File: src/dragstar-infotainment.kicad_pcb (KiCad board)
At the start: 2 copper layers, 100 x 97 mm, 142 parts, among them J1 MiniFit_2x10_F, J1 XT60-M, J10 Conn_01x01_Socket, J100 Conn_01x01_Socket, J101 1217080-1, J102 1217080-1, J103 1217080-1, J104 1217080-1, J105 1217080-1, J106 1217080-1, J107 1217080-1, J108 1217080-1, J109 1217080-1, J11 Conn_01x01_Socket, J110 1217080-1, J111 1217080-1, J112 1217080-1, J12 Conn_01x01_Socket, J13 Conn_01x01_Socket, J14 Conn_01x01_Socket, J15 Conn_01x01_Socket, J16 Conn_01x01_Socket, J17 Conn_01x01_Socket, J18 Conn_01x01_Socket, J19 Conn_01x01_Socket, J20 Conn_01x01_Socket, J21 Conn_01x01_Socket, J22 Conn_01x01_Socket, J23 Conn_01x01_Socket, J24 Conn_01x01_Socket, J25 Conn_01x01_Socket, J26 Conn_01x01_Socket, J27 Conn_01x01_Socket, J28 Conn_01x01_Socket, J29 Conn_01x01_Socket, J3 Conn_01x01_Socket, J30 Conn_01x01_Socket, J31 Conn_01x01_Socket, J32 Conn_01x01_Socket, J33 Conn_01x01_Socket, J34 Conn_01x01_Socket, J35 Conn_01x01_Socket, J36 Conn_01x01_Socket, J37 Conn_01x01_Socket, J38 Conn_01x01_Socket, J39 Conn_01x01_Socket, J4 1217080-1, J4 Conn_01x01_Socket, J40 Conn_01x01_Socket, J41 MiniFit_2x03_F, J42 MiniFit_2x03_F, J43 MiniFit_2x03_F, J44 MiniFit_2x03_F, J45 MiniFit_2x04_M, J46 MiniFit_2x02_F, J47 MiniFit_2x04_F, J5 Conn_01x01_Socket, J50 USB_A, J51 MiniFit_2x01_M, J52 MiniFit_2x01_M, J53 MiniFit_2x03_F, J6 Conn_01x01_Socket, J69 MiniFit_2x04_M, J7 Conn_01x01_Socket, J8 Conn_01x01_Socket, J84 MiniFit_2x02_M, J85 MiniFit_2x03_M, J86 MiniFit_2x01_F, J87 MiniFit_2x01_F, J88 MiniFit_2x04_M, J89 1217080-1, J9 Conn_01x01_Socket, J91 Barrel_Jack, J92 MiniFit_2x03_M, J93 MiniFit_2x03_M, J94 Barrel_Jack, J96 MiniFit_2x03_M, J97 MiniFit_2x03_M, J98 Conn_01x01_Socket, J99 Conn_01x01_Socket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

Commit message: simplify circuit diagram. Remove unecessary features; Split board into two components|
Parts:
- removed D10, D11, D12, D9: US1M, Diode_SMD:D_SMA
- removed the J1 at (118.2, 148.0)
- removed the J1 at (108.6, 66.6)
- removed J100, J14, J15, J16, J17, J18, J19, J20, J21, J22, J23, J24, J25, J26, J27, J28, J29, J30, J31, J32, J33, J34, J35, J36, J37, J40, J98, J99: Conn_01x01_Socket, Connector_Pin:Pin_D1.0mm_L10.0mm
- removed J101, J102, J103, J104, J105, J106, J107, J108, J109, J110, J111, J112, J89: 1217080-1, SamacSys_Parts:1217080-1
- removed the J4 at (125.0, 150.8)
- removed the J4 at (112.8, 77.2)
- removed J41, J42, J53: MiniFit_2x03_F, Connector_Molex:Molex_Mini-Fit_Jr_5566-06A_2x03_P4.20mm_Vertical
- removed J45, J88: MiniFit_2x04_M, Connector_Molex:Molex_Mini-Fit_Jr_5566-08A_2x04_P4.20mm_Vertical
- removed J46: MiniFit_2x02_F, Connector_Molex:Molex_Mini-Fit_Jr_5566-04A_2x02_P4.20mm_Vertical
- removed J47: MiniFit_2x04_F, Connector_Molex:Molex_Mini-Fit_Jr_5566-08A_2x04_P4.20mm_Vertical
- removed J50: USB_A, Connector_USB:USB_A_Molex_67643_Horizontal
- removed J51, J52: MiniFit_2x01_M, Connector_Molex:Molex_Mini-Fit_Jr_5566-02A_2x01_P4.20mm_Vertical
- removed J84: MiniFit_2x02_M, Connector_Molex:Molex_Mini-Fit_Jr_5566-04A_2x02_P4.20mm_Vertical
- removed J85, J92, J93, J96, J97: MiniFit_2x03_M, Connector_Molex:Molex_Mini-Fit_Jr_5566-06A_2x03_P4.20mm_Vertical
- removed J86, J87: MiniFit_2x01_F, Connector_Molex:Molex_Mini-Fit_Jr_5566-02A_2x01_P4.20mm_Vertical
- removed J91, J94: Barrel_Jack, Connector_BarrelJack:BarrelJack_CUI_PJ-063AH_Horizontal
- removed the R2 at (132.7, 123.5)
- removed the R2 at (132.6, 117.8)
- removed the R3 at (126.3, 118.8)
- removed the R3 at (132.7, 125.8)
- removed R6, R7: 10K, Resistor_SMD:R_1206_3216Metric_Pad1.30x1.75mm_HandSolder
- removed R8, R9: 470R, Resistor_THT:R_Axial_DIN0204_L3.6mm_D1.6mm_P5.08mm_Horizontal
- added A1: Mini360_3A, Local Footprints:Mini360_DC_DC_Buck_Converter, F.Cu at (42.8, 124.2)
- added A2: Mini360_3A, Local Footprints:Mini360_DC_DC_Buck_Converter, F.Cu at (42.8, 137.2)
- added C1: 0.01µF, Capacitor_SMD:C_1206_3216Metric_Pad1.33x1.80mm_HandSolder, F.Cu at (69.5, 140.9)
- added C2: 100µF, Capacitor_SMD:C_Elec_8x6.2, F.Cu at (77.8, 133.2)
- added C3: 0.1µF, Capacitor_SMD:C_1206_3216Metric_Pad1.33x1.80mm_HandSolder, B.Cu at (80.2, 135.7)
- added C4: 0.1µF, Capacitor_SMD:C_1206_3216Metric_Pad1.33x1.80mm_HandSolder, B.Cu at (76.0, 144.4)
- added C5: 100µF, Capacitor_SMD:C_Elec_8x6.2, F.Cu at (210.2, 55.2)
- added C6: 0.1µF, Capacitor_SMD:C_1206_3216Metric_Pad1.33x1.80mm_HandSolder, F.Cu at (216.8, 57.2)
- added C7: 100µF, Capacitor_SMD:C_Elec_8x6.2, F.Cu at (62.8, 63.7)
- added C8: 22µF, Capacitor_SMD:C_Elec_6.3x5.4, F.Cu at (62.5, 54.0)
- added D30: US1M, Diode_SMD:D_SMA, B.Cu at (93.1, 59.4)
- added D31: 2.7V, Diode_THT:D_DO-35_SOD27_P7.62mm_Horizontal, F.Cu at (110.5, 61.2)
- added D32: US1M, Diode_SMD:D_SMA, F.Cu at (64.8, 119.7)
- added D33: US1M, Diode_SMD:D_SMA, F.Cu at (64.8, 123.4)
- added D34: US1M, Diode_SMD:D_SMA, F.Cu at (64.8, 126.9)
- added D35: US1M, Diode_SMD:D_SMA, F.Cu at (64.8, 140.2)
- added D36: US1M, Diode_SMD:D_SMA, F.Cu at (64.8, 136.8)
- added D37: US1M, Diode_SMD:D_SMA, F.Cu at (64.8, 133.2)
- added H1: MountingHole_Pad, MountingHole:MountingHole_3.2mm_M3_DIN965_Pad, F.Cu at (109.8, 54.2)
- added H2: MountingHole_Pad, MountingHole:MountingHole_3.2mm_M3_DIN965_Pad, F.Cu at (109.8, 144.2)
- added H3: MountingHole_Pad, MountingHole:MountingHole_3.2mm_M3_DIN965_Pad, F.Cu at (44.8, 54.2)
- added H4: MountingHole_Pad, MountingHole:MountingHole_3.2mm_M3_DIN965_Pad, F.Cu at (44.8, 144.2)
- added J1: Conn_01x01, TestPoint:TestPoint_THTPad_D2.5mm_Drill1.2mm, F.Cu at (74.5, 103.0)
- added J2: Conn_01x01, TestPoint:TestPoint_THTPad_D2.5mm_Drill1.2mm, F.Cu at (74.5, 112.0)
- added J4: Conn_01x01, TestPoint:TestPoint_THTPad_D2.5mm_Drill1.2mm, F.Cu at (70.2, 99.3)
- added J61: Conn_01x01, MountingHole:MountingHole_3.2mm_M3_DIN965_Pad, F.Cu at (53.9, 54.5)
- added J62: Conn_01x01, MountingHole:MountingHole_3.2mm_M3_DIN965_Pad, F.Cu at (84.0, 89.0)
- added J63: Conn_01x01, TestPoint:TestPoint_THTPad_D2.5mm_Drill1.2mm, F.Cu at (80.9, 57.3)
- added J64: 1217080-1, SamacSys_Parts:1217080-1, F.Cu at (72.8, 86.6)
- added J65: 1217080-1, SamacSys_Parts:1217080-1, F.Cu at (72.8, 78.4)
- added J66: 1217080-1, SamacSys_Parts:1217080-1, F.Cu at (89.5, 98.0)
- added J67: 1217080-1, SamacSys_Parts:1217080-1, F.Cu at (89.5, 128.0)
- added J68: 1217080-1, SamacSys_Parts:1217080-1, F.Cu at (89.5, 108.0)
- added J70: 1217080-1, SamacSys_Parts:1217080-1, F.Cu at (97.7, 138.0)
- added J71: 1217080-1, SamacSys_Parts:1217080-1, F.Cu at (97.7, 98.0)
- added J72: 1217080-1, SamacSys_Parts:1217080-1, F.Cu at (97.7, 128.0)
- added J73: 1217080-1, SamacSys_Parts:1217080-1, F.Cu at (97.7, 108.0)
- added J74: 1217080-1, SamacSys_Parts:1217080-1, F.Cu at (97.8, 118.0)
- added J75: 1217080-1, SamacSys_Parts:1217080-1, F.Cu at (89.5, 138.0)
- added L2: 22µH, Inductor_THT:L_Toroid_Vertical_L17.8mm_W9.7mm_P7.11mm_Pulse_B, F.Cu at (69.4, 63.7)
- added R2: 1K, Resistor_SMD:R_1206_3216Metric_Pad1.30x1.75mm_HandSolder, B.Cu at (68.0, 132.0)
- added R21: 10K, Resistor_SMD:R_1206_3216Metric_Pad1.30x1.75mm_HandSolder, F.Cu at (204.0, 79.5)
- added R23: 10K, Resistor_SMD:R_1206_3216Metric_Pad1.30x1.75mm_HandSolder, B.Cu at (95.5, 64.0)
- added R3: 10K, Resistor_SMD:R_1206_3216Metric_Pad1.30x1.75mm_HandSolder, B.Cu at (61.0, 130.6)
- added RV1: 10K-50K, Potentiometer_THT:Potentiometer_Bourns_3386P_Vertical, F.Cu at (55.5, 145.5)
- D1, D2, D7, R5: moved to B.Cu
- D13, D4: footprint Diode_SMD:D_MiniMELF -> Diode_THT:D_DO-35_SOD27_P7.62mm_Horizontal
- D14: value US1M -> 1N4001; footprint Diode_SMD:D_SMA -> Diode_THT:D_DO-41_SOD81_P10.16mm_Horizontal; moved to F.Cu
- D15, D16: value 2.7V -> 1N4001; footprint Diode_SMD:D_MiniMELF -> Diode_THT:D_DO-41_SOD81_P10.16mm_Horizontal; moved to F.Cu
- D17: value LED -> 1N4001; footprint LED_THT:LED_D5.0mm -> Diode_THT:D_DO-41_SOD81_P10.16mm_Horizontal
- D18, D19: value LED -> 2.7V; footprint LED_THT:LED_D5.0mm -> Diode_THT:D_DO-35_SOD27_P7.62mm_Horizontal
- D20: value LED -> US1M; footprint LED_THT:LED_D5.0mm -> Diode_SMD:D_SMA
- D21: value LED Green -> US1M; footprint LED_THT:LED_D5.0mm -> Diode_SMD:D_SMA
- D22: value LED Blue -> US1M; footprint LED_THT:LED_D5.0mm -> Diode_SMD:D_SMA
- D23: value LED Red -> 10V; footprint LED_THT:LED_D5.0mm -> Diode_THT:D_DO-35_SOD27_P7.62mm_Horizontal
- D24: value LED Yellow -> LED_Dual_AKA (Green, Red); footprint LED_THT:LED_D5.0mm -> LED_THT:LED_D5.0mm-3
- D26: value US1M -> LED Blue; footprint Diode_SMD:D_SMA -> LED_THT:LED_D5.0mm; moved to F.Cu
- D27: value 2.7V -> LED Red; footprint Diode_SMD:D_MiniMELF -> LED_THT:LED_D5.0mm; moved to F.Cu
- D28: value 10V -> LED Green; footprint Diode_SMD:D_MiniMELF -> LED_THT:LED_D5.0mm
- D3, D6: footprint Diode_SMD:D_MiniMELF -> Diode_THT:D_DO-35_SOD27_P7.62mm_Horizontal; moved to F.Cu
- D8: value US1M -> 2.7V; footprint Diode_SMD:D_SMA -> Diode_THT:D_DO-35_SOD27_P7.62mm_Horizontal
- J10, J11, J12, J3, J5, J6, J7, J8, J9: value Conn_01x01_Socket -> Conn_01x01; footprint Connector_Pin:Pin_D1.0mm_L10.0mm -> TestPoint:TestPoint_THTPad_D2.5mm_Drill1.2mm; moved to F.Cu
- J13: value Conn_01x01_Socket -> XT60-M; footprint Connector_Pin:Pin_D1.0mm_L10.0mm -> Local Footprints:AMASS_XT60PW-M_1x02_P7.20mm_Horizontal_Short; moved to F.Cu
- J38, J39: value Conn_01x01_Socket -> JST XH 6 Pins; footprint Connector_Pin:Pin_D1.0mm_L10.0mm -> Connector_JST:JST_XH_B6B-XH-A_1x06_P2.50mm_Vertical
- J43, J44: value MiniFit_2x03_F -> Conn_01x01; footprint Connector_Molex:Molex_Mini-Fit_Jr_5566-06A_2x03_P4.20mm_Vertical -> TestPoint:TestPoint_THTPad_D2.5mm_Drill1.2mm
- J69: value MiniFit_2x04_M -> 1217080-1; footprint Connector_Molex:Molex_Mini-Fit_Jr_5566-08A_2x04_P4.20mm_Vertical -> SamacSys_Parts:1217080-1
- Q5, Q6: value 2N7002 -> AO3413; moved to F.Cu
- Q7: value BC557 -> 2N7002; footprint Package_TO_SOT_THT:TO-92_Inline -> Package_TO_SOT_SMD:SOT-23; moved to B.Cu
- R10, R11: value 470R -> 10K; footprint Resistor_THT:R_Axial_DIN0204_L3.6mm_D1.6mm_P5.08mm_Horizontal -> Resistor_SMD:R_1206_3216Metric_Pad1.30x1.75mm_HandSolder
- R12: value 680R -> 10K; footprint Resistor_THT:R_Axial_DIN0204_L3.6mm_D1.6mm_P5.08mm_Horizontal -> Resistor_SMD:R_1206_3216Metric_Pad1.30x1.75mm_HandSolder
- R13: value 680R -> 100; footprint Resistor_THT:R_Axial_DIN0204_L3.6mm_D1.6mm_P5.08mm_Horizontal -> Resistor_SMD:R_1206_3216Metric_Pad1.30x1.75mm_HandSolder
- R14: value 680R -> 1.5K; footprint Resistor_THT:R_Axial_DIN0204_L3.6mm_D1.6mm_P5.08mm_Horizontal -> Resistor_SMD:R_1206_3216Metric_Pad1.30x1.75mm_HandSolder
- R17: value 10K -> 680R; footprint Resistor_SMD:R_1206_3216Metric_Pad1.30x1.75mm_HandSolder -> Resistor_THT:R_Axial_DIN0204_L3.6mm_D1.6mm_P5.08mm_Horizontal; moved to F.Cu
- R18: value 100 -> 680R; footprint Resistor_SMD:R_1206_3216Metric_Pad1.30x1.75mm_HandSolder -> Resistor_THT:R_Axial_DIN0204_L3.6mm_D1.6mm_P5.08mm_Horizontal
- R19: value 1.5K -> 680R; footprint Resistor_SMD:R_1206_3216Metric_Pad1.30x1.75mm_HandSolder -> Resistor_THT:R_Axial_DIN0204_L3.6mm_D1.6mm_P5.08mm_Horizontal
- R20: value 10K -> 680R; footprint Resistor_SMD:R_1206_3216Metric_Pad1.30x1.75mm_HandSolder -> Resistor_THT:R_Axial_DIN0204_L3.6mm_D1.6mm_P5.08mm_Horizontal
- moved J69 344.8 mm to (89.5, 118.0)
- moved D20 290.7 mm to (211.5, 84.5)
- moved D19 290.5 mm to (197.6, 73.8), turned to 90 degrees
- moved D18 272.4 mm to (205.1, 63.8), turned to 180 degrees
- moved D17 262.6 mm to (200.0, 48.0), turned to -90 degrees
- moved R11 260.6 mm to (203.4, 66.5)
- moved R10 250.2 mm to (218.3, 68.3), turned to 90 degrees
- moved J43 245.3 mm to (209.6, 80.8), turned to 90 degrees
- moved J44 234.6 mm to (214.1, 80.8), turned to 90 degrees
- moved D25 215.4 mm to (220.8, 108.3), turned to 180 degrees
- moved D23 210.2 mm to (197.3, 82.2)
- moved D22 204.9 mm to (198.2, 87.2), turned to 90 degrees
- moved R14 203.3 mm to (197.6, 77.5), turned to -90 degrees
- moved R13 202.0 mm to (200.1, 77.3), turned to 90 degrees
- moved R12 201.2 mm to (200.1, 72.0), turned to -90 degrees
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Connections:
- D13 pad 1: /Main board/XOR 74LS00/B -> /Accessories/XOR 74LS00/A
- D14 pad 1: AuxSwitch -> RBlinker
- D14 pad 2: Net-(D14-A) -> Hazard
- D15 pad 1: Net-(D15-K) -> RBlinker
- D15 pad 2: GND -> Hazard
- D16 pad 1: Net-(D16-K) -> LBlinker
- D16 pad 2: GND -> Hazard
- D17 pad 1: GNDDash -> LBlinker
- D17 pad 2: Net-(D17-A) -> Hazard
- D18 pad 1: HazardLed -> /Accessories/XOR 74LS00/B
- D18 pad 2: Net-(D18-A) -> GND
- D19 pad 1: GNDDash -> Net-(D19-K)
- D19 pad 2: Net-(D19-A) -> GND
- D20 pad 1: GNDDash -> AuxLed2
- D20 pad 2: Net-(D20-A) -> AuxHBeam
- D21 pad 1: GNDDash -> AuxLed1
- D21 pad 2: Net-(D21-A) -> AuxHBeam
- D22 pad 1: GNDDash -> AuxLed1
- D22 pad 2: Net-(D22-A) -> AuxLBeam
- D23 pad 1: GNDDash -> Net-(D23-K)
- D24 pad 1: GNDDash -> Net-(D24-A1)
- D24 pad 2: Net-(D24-A) -> GNDDash
- D26 pad 1: +BATT -> GNDDash
- D27 pad 1: Net-(D27-K) -> GNDDash
- D27 pad 2: GND -> Net-(D27-A)
- D28 pad 1: Net-(D28-K) -> GNDDash
- D4 pad 1: PLightSignal -> Net-(D4-K)
- D7 pad 1: RBlinker -> AuxSwitch
- D7 pad 2: Hazard -> Net-(D7-A)
- D8 pad 1: RBlinker -> Net-(D8-K)
- D8 pad 2: Hazard -> GND
- J10 pad 1: Hazard -> AuxLBeam
- J11 pad 1: LBlinker -> AuxHBeam
- J12 pad 1: RBlinker -> AuxSwitch
- J13 pad 1: Key -> GND
- J3 pad 1: AuxLBeam -> Key
- J38 pad 1: GNDDash -> VInst
- J39 pad 1: PLight -> LBlinker
- J44 pad 1: VInst -> GND
- J5 pad 1: AuxHBeam -> HBeam
- J6 pad 1: HBeam -> PLight
- J69 pad 1: Accessory -> VLight
- J69 pad 2: HBeam -> VLight
- J7 pad 1: AuxBeams -> +5V
- J8 pad 1: AuxSwitch -> VOutlet
- J9 pad 1: HazardLed -> GNDDash
- K2 pad A1: Net-(D14-A) -> Net-(D7-A)
- K3 pad 14: +BATT -> MainRelay
- K3 pad A1: +BATT -> MainRelay
- K3 pad A2: Net-(D26-A) -> /Main board/Power Delivery/RelayGnd
- Q1 pad 3: GndDimmer -> Net-(Q1-D)
- Q2 pad 1: PLightSignal -> Net-(D4-K)
- Q2 pad 2: GndDimmer -> Net-(Q1-D)
- Q4 pad 1: Net-(D15-K) -> Net-(D8-K)
- Q4 pad 3: Net-(D14-A) -> Net-(D7-A)
- Q5 pad 1: Net-(D16-K) -> Net-(D19-K)
- Q5 pad 3: GndDimmer -> VInst
- Q6 pad 1: Net-(D27-K) -> Net-(D23-A)
- Q6 pad 2: GND -> LowBat
- Q6 pad 3: Net-(D26-A) -> VInst
- Q7 pad 1: +BATT -> Net-(D31-K)
- Q7 pad 2: Net-(D28-A) -> GND
- Q7 pad 3: LowBat -> /Main board/Power Delivery/RelayGnd
- R10 pad 1: Net-(D19-A) -> PLight
- R10 pad 2: VInst -> /Accessories/XOR 74LS00/A
- R11 pad 1: Net-(D20-A) -> Hazard
- R11 pad 2: VInst -> /Accessories/XOR 74LS00/B
- R12 pad 1: Net-(D21-A) -> /Accessories/XOR 74LS00/O
- R12 pad 2: LBlinker -> Net-(D19-K)
- R13 pad 1: Net-(D22-A) -> Net-(D23-K)
- R13 pad 2: HBeam -> VInst
- R14 pad 1: Net-(D23-A) -> GND
- R14 pad 2: LowBat -> Net-(D23-K)
- R15 pad 1: Net-(D24-A) -> Net-(D24-A2)
- R15 pad 2: AuxBeams -> AuxLed1
- R16 pad 1: Net-(D25-A) -> Net-(D24-A1)
- R16 pad 2: RBlinker -> AuxLed2
- R17 pad 1: Key -> Net-(D25-A)
- R17 pad 2: Net-(D27-K) -> LBlinker
- R18 pad 1: Net-(D28-K) -> Net-(D26-A)
- R18 pad 2: +BATT -> HBeam
- R19 pad 1: GND -> Net-(D27-A)
- R19 pad 2: Net-(D28-K) -> LowBat
- R20 pad 1: GND -> Net-(D28-A)
- R20 pad 2: Net-(D28-A) -> RBlinker
- R5 pad 1: Hazard -> HBeam
- R5 pad 2: /Main board/XOR 74LS00/B -> Net-(D8-K)
- U2 pad 1: PLightSignal -> /Accessories/XOR 74LS00/A
- U2 pad 10: /Main board/XOR 74LS00/B -> /Accessories/XOR 74LS00/B
- U2 pad 12: PLightSignal -> /Accessories/XOR 74LS00/A
- U2 pad 2: /Main board/XOR 74LS00/B -> /Accessories/XOR 74LS00/B
- U2 pad 6: /Main board/XOR 74LS00/O -> /Accessories/XOR 74LS00/O
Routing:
- net +12V: track 26.8 -> 223.5 mm
- net MainRelay: track 0.00 -> 152.0 mm
- net VInst: track 0.00 -> 109.4 mm
- net +5VA: track 0.00 -> 65.6 mm
- net +BATT: track 66.2 -> 10.1 mm
- net GNDDash: track 7.98 -> 62.2 mm
- net Net-(C7-Pad1): track 0.00 -> 51.1 mm
- net +5V: track 17.6 -> 66.6 mm
- net GndDimmer: track 46.7 -> 0.00 mm
- net VLight: track 43.0 -> 84.3 mm
- net VAcc: track 0.00 -> 39.3 mm
- net Killswitch: track 0.00 -> 37.3 mm
- net VOutlet: track 0.00 -> 35.4 mm
- net Key: track 38.4 -> 11.6 mm
- net AuxBeams: track 25.2 -> 0.00 mm
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- added copper zone on F.Cu, net GND
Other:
- board size 100 x 97 mm -> 75 x 100 mm

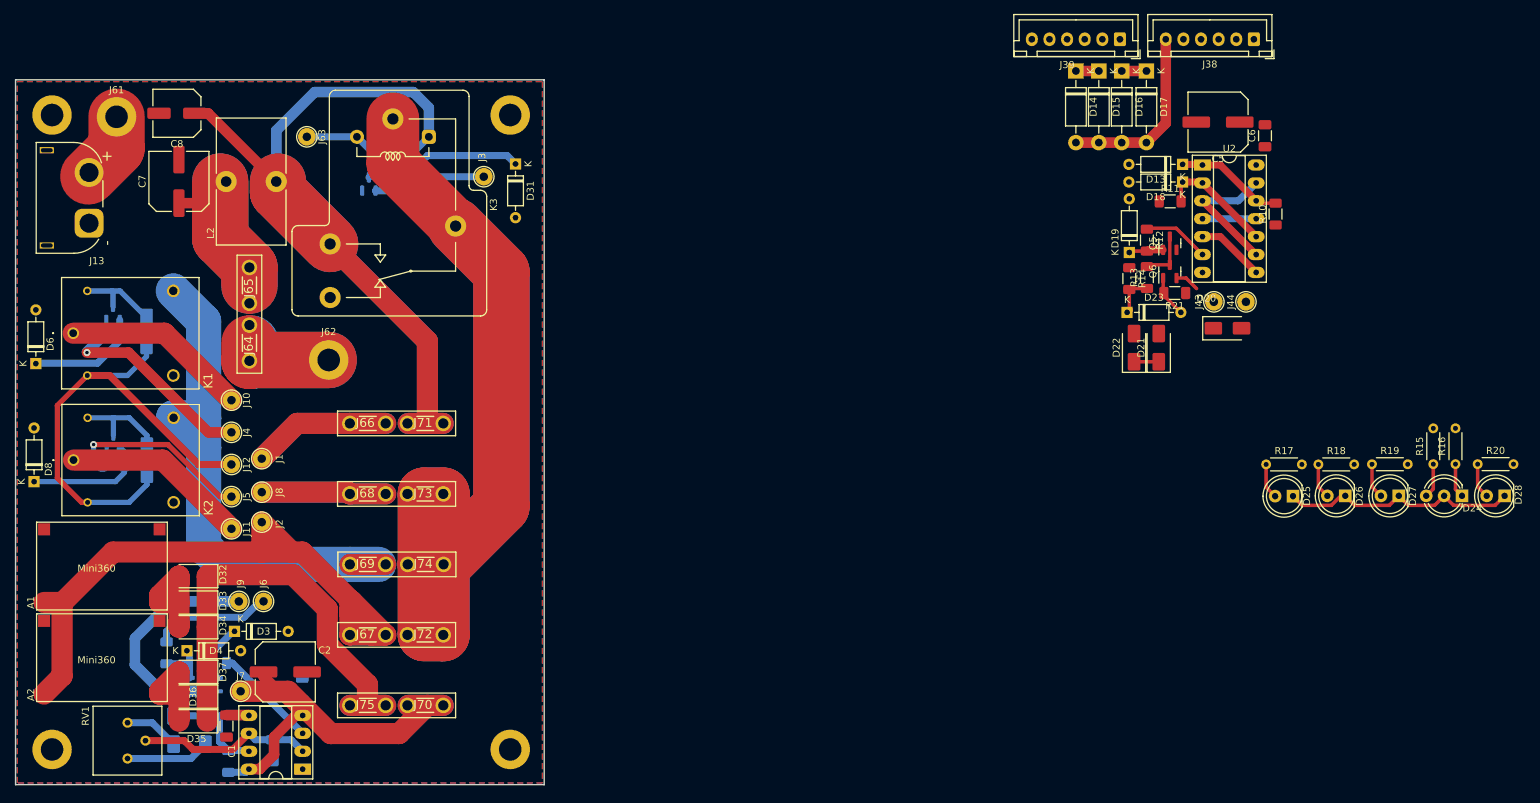
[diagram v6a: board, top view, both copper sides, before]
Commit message: Simplify circuit diagram. Remove unecessary features
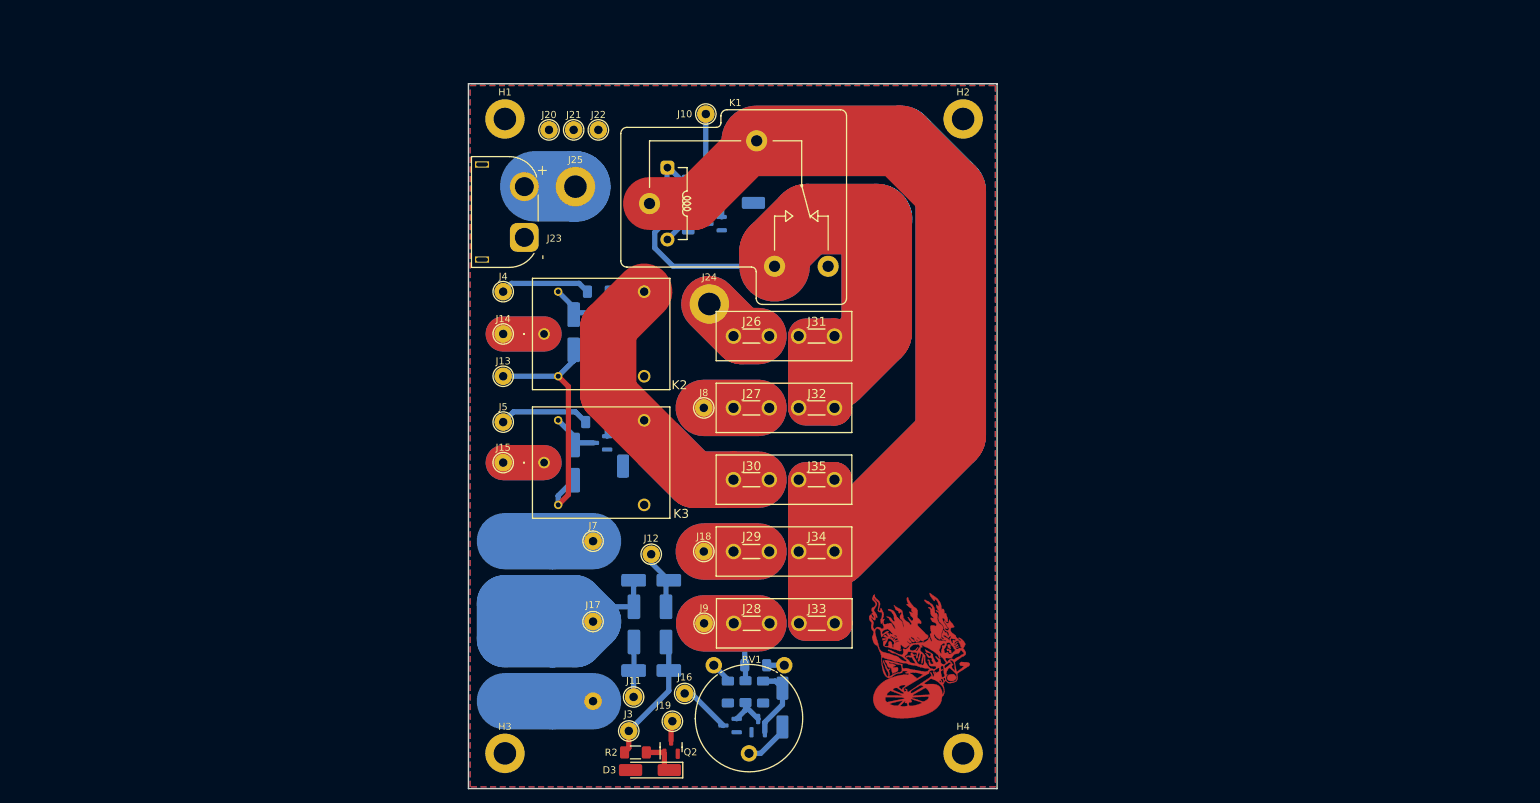
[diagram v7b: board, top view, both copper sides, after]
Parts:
- removed A1, A2: Mini360_3A, Local Footprints:Mini360_DC_DC_Buck_Converter
- removed C1: 0.01µF, Capacitor_SMD:C_1206_3216Metric_Pad1.33x1.80mm_HandSolder
- removed C2, C5, C7: 100µF, Capacitor_SMD:C_Elec_8x6.2
- removed C3, C4, C6: 0.1µF, Capacitor_SMD:C_1206_3216Metric_Pad1.33x1.80mm_HandSolder
- removed C8: 22µF, Capacitor_SMD:C_Elec_6.3x5.4
- removed D17: 1N4001, Diode_THT:D_DO-41_SOD81_P10.16mm_Horizontal
- removed D18, D19, D31: 2.7V, Diode_THT:D_DO-35_SOD27_P7.62mm_Horizontal
- removed D20, D21, D22, D30, D32, D33, D34, D35, D36, D37: US1M, Diode_SMD:D_SMA
- removed D23: 10V, Diode_THT:D_DO-35_SOD27_P7.62mm_Horizontal
- removed D24: LED_Dual_AKA (Green, Red), LED_THT:LED_D5.0mm-3
- removed D25, D28: LED Green, LED_THT:LED_D5.0mm
- removed D26: LED Blue, LED_THT:LED_D5.0mm
- removed D27: LED Red, LED_THT:LED_D5.0mm
- removed J1, J2, J43, J44, J63: Conn_01x01, TestPoint:TestPoint_THTPad_D2.5mm_Drill1.2mm
- removed J38, J39: JST XH 6 Pins, Connector_JST:JST_XH_B6B-XH-A_1x06_P2.50mm_Vertical
- removed J61, J62: Conn_01x01, MountingHole:MountingHole_3.2mm_M3_DIN965_Pad
- removed J64, J65, J66, J67, J68, J69, J70, J71, J72, J73, J74, J75: 1217080-1, SamacSys_Parts:1217080-1
- removed L2: 22µH, Inductor_THT:L_Toroid_Vertical_L17.8mm_W9.7mm_P7.11mm_Pulse_B
- removed Q7: 2N7002, Package_TO_SOT_SMD:SOT-23
- removed R10, R11, R12, R21, R23: 10K, Resistor_SMD:R_1206_3216Metric_Pad1.30x1.75mm_HandSolder
- removed R13: 100, Resistor_SMD:R_1206_3216Metric_Pad1.30x1.75mm_HandSolder
- removed R14: 1.5K, Resistor_SMD:R_1206_3216Metric_Pad1.30x1.75mm_HandSolder
- removed R15, R16, R17, R18, R19, R20: 680R, Resistor_THT:R_Axial_DIN0204_L3.6mm_D1.6mm_P5.08mm_Horizontal
- removed U1: LM555xN, Package_DIP:DIP-8_W7.62mm_Socket_LongPads
- removed U2: 74LS00, Package_DIP:DIP-14_W7.62mm_Socket_LongPads
- added D10: SK510, Diode_SMD:D_SMC_Handsoldering, B.Cu at (115.8, 119.1)
- added D11: US1M, Diode_SMD:D_SMA_Handsoldering, B.Cu at (129.8, 133.1)
- added D12: BZV55C2V7, Diode_SMD:D_MiniMELF_Handsoldering, B.Cu at (148.4, 138.3)
- added D9: SK510, Diode_SMD:D_SMC_Handsoldering, B.Cu at (109.0, 119.1)
- added J14: Conn_01x01, TestPoint:TestPoint_THTPad_D2.5mm_Drill1.2mm, F.Cu at (108.8, 85.3)
- added J15: Conn_01x01, TestPoint:TestPoint_THTPad_D2.5mm_Drill1.2mm, F.Cu at (108.8, 103.6)
- added J16: Conn_01x01, TestPoint:TestPoint_THTPad_D2.5mm_Drill1.2mm, F.Cu at (134.5, 136.3)
- added J17: Conn_01x01, TestPoint:TestPoint_THTPad_D2.5mm_Drill1.2mm, F.Cu at (121.5, 126.1)
- added J18: Conn_01x01, TestPoint:TestPoint_THTPad_D2.5mm_Drill1.2mm, F.Cu at (137.2, 116.2)
- added J19: Conn_01x01, TestPoint:TestPoint_THTPad_D2.5mm_Drill1.2mm, F.Cu at (132.8, 140.2)
- added J20: Conn_01x01, TestPoint:TestPoint_THTPad_D2.5mm_Drill1.2mm, F.Cu at (115.2, 56.4)
- added J21: Conn_01x01, TestPoint:TestPoint_THTPad_D2.5mm_Drill1.2mm, F.Cu at (118.8, 56.4)
- added J22: Conn_01x01, TestPoint:TestPoint_THTPad_D2.5mm_Drill1.2mm, F.Cu at (122.2, 56.4)
- added J23: XT60-M, Local Footprints:AMASS_XT60PW-M_1x02_P7.20mm_Horizontal_Short, F.Cu at (111.8, 71.6)
- added J24: Conn_01x01, MountingHole:MountingHole_3.2mm_M3_DIN965_Pad, F.Cu at (138.0, 81.1)
- added J25: Conn_01x01, MountingHole:MountingHole_3.2mm_M3_DIN965_Pad, F.Cu at (119.0, 64.4)
- added J26: 1217080-1, SamacSys_Parts:1217080-1, F.Cu at (144.0, 85.6)
- added J27: 1217080-1, SamacSys_Parts:1217080-1, F.Cu at (144.0, 95.8)
- added J28: 1217080-1, SamacSys_Parts:1217080-1, F.Cu at (144.0, 126.4)
- added J29: 1217080-1, SamacSys_Parts:1217080-1, F.Cu at (144.0, 116.2)
- added J30: 1217080-1, SamacSys_Parts:1217080-1, F.Cu at (144.0, 106.0)
- added J31: 1217080-1, SamacSys_Parts:1217080-1, F.Cu at (153.2, 85.6)
- added J32: 1217080-1, SamacSys_Parts:1217080-1, F.Cu at (153.2, 95.8)
- added J33: 1217080-1, SamacSys_Parts:1217080-1, F.Cu at (153.2, 126.4)
- added J34: 1217080-1, SamacSys_Parts:1217080-1, F.Cu at (153.2, 116.2)
- added J35: 1217080-1, SamacSys_Parts:1217080-1, F.Cu at (153.2, 106.0)
- added R6: 1.5K, Resistor_SMD:R_1206_3216Metric_Pad1.30x1.75mm_HandSolder, B.Cu at (140.6, 136.1)
- added R7: 10K, Resistor_SMD:R_1206_3216Metric_Pad1.30x1.75mm_HandSolder, B.Cu at (122.2, 79.3)
- added R8: 10K, Resistor_SMD:R_1206_3216Metric_Pad1.30x1.75mm_HandSolder, B.Cu at (122.0, 97.8)
- D1, D5: footprint Diode_SMD:D_SMA -> Diode_SMD:D_SMA_Handsoldering
- D13, D4, D6: value 2.7V -> US1M; footprint Diode_THT:D_DO-35_SOD27_P7.62mm_Horizontal -> Diode_SMD:D_SMA_Handsoldering; moved to B.Cu
- D14, D16: value 1N4001 -> BZV55C2V7; footprint Diode_THT:D_DO-41_SOD81_P10.16mm_Horizontal -> Diode_SMD:D_MiniMELF_Handsoldering; moved to B.Cu
- D15: value 1N4001 -> US1M; footprint Diode_THT:D_DO-41_SOD81_P10.16mm_Horizontal -> Diode_SMD:D_SMA_Handsoldering; moved to B.Cu
- D2: value US1M -> BZV55C2V7; footprint Diode_SMD:D_SMA -> Diode_SMD:D_MiniMELF_Handsoldering
- D3: value 2.7V -> BZV55C2V7; footprint Diode_THT:D_DO-35_SOD27_P7.62mm_Horizontal -> Diode_SMD:D_MiniMELF_Handsoldering
- D7: value US1M -> SK510; footprint Diode_SMD:D_SMA -> Diode_SMD:D_SMC_Handsoldering
- D8: value 2.7V -> SK510; footprint Diode_THT:D_DO-35_SOD27_P7.62mm_Horizontal -> Diode_SMD:D_SMC_Handsoldering; moved to B.Cu
- J13: value XT60-M -> Conn_01x01; footprint Local Footprints:AMASS_XT60PW-M_1x02_P7.20mm_Horizontal_Short -> TestPoint:TestPoint_THTPad_D2.5mm_Drill1.2mm
- J6: moved to B.Cu
- K1: value LEG-12 -> RAYEX-L90; footprint Local Footprints:LEG12 -> Local Footprints:Relay_SPDT_RAYEX-L90
- K3: value RAYEX-L90 -> LEG-12; footprint Local Footprints:Relay_SPDT_RAYEX-L90 -> Local Footprints:LEG12
- Q2: moved to F.Cu
- Q5, Q6: value AO3413 -> 2N7002; moved to B.Cu
- R1: value 1K -> 10K
- R2: value 1K -> 10K; moved to F.Cu
- R3, R4: value 10K -> 1.5K
- R5: value 10K -> 11K
- RV1: value 10K-50K -> 5K; footprint Potentiometer_THT:Potentiometer_Bourns_3386P_Vertical -> Potentiometer_THT:Potentiometer_Piher_PT-15-V02_Vertical
- moved H4 129.3 mm to (174.0, 144.8), turned to 0 degrees
- moved H3 111.0 mm to (109.0, 144.8), turned to 0 degrees
- moved H2 110.1 mm to (174.0, 54.8), turned to 0 degrees
- moved R1 107.1 mm to (139.3, 64.5), turned to 180 degrees
- moved D2 105.9 mm to (141.5, 66.7), turned to 0 degrees
- moved Q3 105.3 mm to (140.9, 140.9), turned to 180 degrees
- moved D1 104.3 mm to (135.0, 67.0), turned to -90 degrees
- moved R4 102.4 mm to (144.6, 132.3), turned to 180 degrees
- moved Q4 99.9 mm to (144.9, 140.9)
- moved R5 97.6 mm to (145.6, 136.1), turned to 90 degrees
- moved Q1 96.9 mm to (138.8, 69.7)
- moved D15 92.9 mm to (118.8, 103.6), turned to 90 degrees
- moved D6 92.6 mm to (127.3, 126.5)
- moved D13 89.6 mm to (118.8, 85.1), turned to 90 degrees
- moved D16 88.6 mm to (125.8, 101.3)
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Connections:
- D1 pad 1: Net-(D1-K) -> MainRelay
- D1 pad 2: Net-(D1-A) -> /Main board/RelayGnd
- D13 pad 1: /Accessories/XOR 74LS00/A -> AuxSwitch
- D13 pad 2: GND -> Net-(D13-A)
- D14 pad 1: RBlinker -> Net-(D14-K)
- D14 pad 2: Hazard -> GND
- D15 pad 1: RBlinker -> AuxSwitch
- D15 pad 2: Hazard -> Net-(D15-A)
- D16 pad 1: LBlinker -> Net-(D16-K)
- D16 pad 2: Hazard -> GND
- D2 pad 1: Net-(D1-A) -> Net-(D2-K)
- D2 pad 2: Net-(D2-A) -> GND
- D4 pad 1: Net-(D4-K) -> Hazard
- D4 pad 2: GND -> HazardLedReturn
- D5 pad 1: AuxSwitch -> PLight
- D5 pad 2: Net-(D5-A) -> HazardLedReturn
- D6 pad 1: Net-(D6-K) -> HazardLed
- D6 pad 2: GND -> Hazard
- D7 pad 1: AuxSwitch -> LBlinker
- D7 pad 2: Net-(D7-A) -> Hazard
- D8 pad 1: Net-(D8-K) -> LBlinker
- D8 pad 2: GND -> Hazard
- J10 pad 1: AuxLBeam -> Key
- J11 pad 1: AuxHBeam -> HazardLed
- J12 pad 1: AuxSwitch -> HazardLedReturn
- J13 pad 1: GND -> AuxSwitch
- J3 pad 1: Key -> PLight
- J6 pad 1: PLight -> LBlinker
- J7 pad 1: +5V -> RBlinker
- J8 pad 1: VOutlet -> VAcc
- J9 pad 1: GNDDash -> VInst
- K1 pad A1: Net-(D5-A) -> MainRelay
- K1 pad A2: AuxSwitch -> /Main board/RelayGnd
- K2 pad A1: Net-(D7-A) -> Net-(D13-A)
- K2 pad COM: AuxHBeam -> AuxLBeam
- K3 pad A1: MainRelay -> Net-(D15-A)
- K3 pad A2: /Main board/Power Delivery/RelayGnd -> AuxSwitch
- Q1 pad 1: Net-(D3-K) -> Net-(D2-K)
- Q1 pad 3: Net-(Q1-D) -> /Main board/RelayGnd
- Q2 pad 1: Net-(D4-K) -> Net-(D3-K)
- Q2 pad 2: Net-(Q1-D) -> GND
- Q3 pad 1: Net-(D6-K) -> Net-(Q3-G)
- Q3 pad 3: Net-(D5-A) -> LowBat
- Q4 pad 1: Net-(D8-K) -> Net-(D12-A)
- Q4 pad 3: Net-(D7-A) -> Net-(Q3-G)
- Q5 pad 1: Net-(D19-K) -> Net-(D14-K)
- Q5 pad 2: HazardLed -> GND
- Q5 pad 3: VInst -> Net-(D13-A)
- Q6 pad 1: Net-(D23-A) -> Net-(D16-K)
- Q6 pad 2: LowBat -> GND
- Q6 pad 3: VInst -> Net-(D15-A)
- R1 pad 1: Net-(D1-A) -> Key
- R1 pad 2: +5V -> Net-(D2-K)
- R2 pad 1: Net-(D3-K) -> PLight
- R2 pad 2: Net-(U1-Q) -> Net-(D3-K)
- R3 pad 1: PLight -> Net-(Q3-G)
- R3 pad 2: Net-(D4-K) -> VInst
- R4 pad 1: LBeam -> Net-(R4-Pad1)
- R4 pad 2: Net-(D6-K) -> VInst
- R5 pad 1: HBeam -> GND
- R5 pad 2: Net-(D8-K) -> Net-(D12-A)
- RV1 pad 1: Net-(D2-A) -> Net-(R6-Pad2)
- RV1 pad 3: Net-(D1-K) -> Net-(R4-Pad1)
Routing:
- net +12V: track 223.5 -> 346.8 mm
- net VInst: track 109.4 -> 24.4 mm
- net +5V: track 66.6 -> 0.00 mm
- net +5VA: track 65.6 -> 0.00 mm
- net GNDDash: track 62.2 -> 2.81 mm
- net Net-(C7-Pad1): track 51.1 -> 0.00 mm
- net MainRelay: track 152.0 -> 189.0 mm
- net AuxSwitch: track 69.7 -> 36.3 mm
- net VAcc: track 39.3 -> 15.5 mm
- net Net-(D31-K): track 22.4 -> 0.00 mm
- net Hazard: track 25.8 -> 47.8 mm
- net VOutlet: track 35.4 -> 15.5 mm
- net Killswitch: track 37.3 -> 17.7 mm
- net Net-(U2-Pad13): track 19.5 -> 0.00 mm
- net Net-(D12-K): track 24.8 -> 6.69 mm
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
